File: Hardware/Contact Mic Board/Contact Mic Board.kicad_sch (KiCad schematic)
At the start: 29 parts, among them U1 ES8388, U2 MCP6002-xMC, U3 MCP6002-xMC

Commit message: revised contact mic board
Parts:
- removed C2, C4, C8: 0.1uF, symbol Device:C_Small
- removed C6: 10uF, symbol Device:C_Small
- removed R6: 100k, symbol Device:R
- added C15, C17, C2, C4, C6, C8: 10uF, symbol Device:C_Polarized_Small_US
- added C16, C18: 0.1uF, symbol Device:C_Small
- added FB1: FerriteBead_Small, symbol Device:FerriteBead_Small
- added J1: Conn_01x08_Pin, symbol Connector:Conn_01x08_Pin
- added R11, R12, R13, R14: 33, symbol Device:R_Small_US
- added R6: 100k, symbol Device:R_Small_US
- C5: value 4.7uF -> 0.1uF
- R1, R10, R2, R3, R4, R5, R7, R8, R9: symbol Device:R -> Device:R_Small_US
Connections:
- net GND: now also C1.1, C3.1, C5.1, C15.2, C16.2, C17.2, C18.2, C2.2, C4.2, C6.2, C8.2, J1.8 (Pin_8); no longer C1.2, C3.2, C5.2
- net at C11.2, C12.2, R3.2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: now also C17.1, C18.1
- net at U1.1 (MCLK): now also R11.2
- net at U1.27 (CDATA): now also J1.6 (Pin_6)
- net at U1.28 (CCLK): now also J1.7 (Pin_7)
- net at U1.5 (SCLK): now also R12.2
- net at U1.7 (LRCK): now also R13.2
- net at U1.8 (ASDOUT): now also R14.2
- net at C10.2, U2.1: now also R6.1
- net at R7.1, U2.2 (-): now also R6.2
- removed net +3.3V: C1.1, C3.1, C5.1, C7.2, U1.10 (VREF), U1.16 (HPVDD), U1.17 (AVDD), U1.19 (ADCVREF), U1.2 (DVDD), U1.3 (PVDD)
- new net: C8.1, U1.10 (VREF)
- new net: C1.2, C2.1, C3.2, C6.1, C7.2, FB1.2, J1.1 (Pin_1), U1.16 (HPVDD), U1.2 (DVDD), U1.3 (PVDD)
- new net: C4.1, C5.2, FB1.1, U1.17 (AVDD)
- new net: C15.1, C16.1, U1.19 (ADCVREF)
- new net: J1.2 (Pin_2), R11.1
- new net: J1.4 (Pin_4), R13.1
- new net: J1.3 (Pin_3), R12.1
- new net: J1.5 (Pin_5), R14.1
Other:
- moved on the sheet: C10, C9

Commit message: drafted contact mic pcb layout
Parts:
- removed U3: MCP6002-xMC, Package_DFN_QFN:DFN-8-1EP_3x2mm_P0.5mm_EP1.75x1.45mm, symbol Amplifier_Operational:MCP6002-xMC
- added unit 3 of U2
- added unit 2 of U2
- C1, C10, C11, C12, C13, C16, C18, C3, C9, R1, R10, R11, R12, R13, R14, R2, R3, R4, R7, R8, R9: footprint (none) -> Capacitor_SMD:C_0402_1005Metric
- C14: renamed from C8; footprint (none) -> Capacitor_SMD:C_0603_1608Metric
- C15, C17, C2, FB1: footprint (none) -> Capacitor_SMD:C_0603_1608Metric
- C4: renamed from C6; footprint (none) -> Capacitor_SMD:C_0603_1608Metric
- C5: renamed from C7; footprint (none) -> Capacitor_SMD:C_0402_1005Metric
- C6: renamed from C5; footprint (none) -> Capacitor_SMD:C_0402_1005Metric
- C7: renamed from C4; footprint (none) -> Capacitor_SMD:C_0603_1608Metric
- C8: renamed from C14; footprint (none) -> Capacitor_SMD:C_0402_1005Metric
- J1: value Conn_01x08_Pin -> Conn_01x09_Pin; footprint (none) -> Connector_JST:JST_GH_SM09B-GHS-TB_1x09-1MP_P1.25mm_Horizontal; symbol Connector:Conn_01x08_Pin -> Connector:Conn_01x09_Pin
- MIC1, MIC2: footprint (none) -> Connector_PinHeader_2.54mm:PinHeader_1x02_P2.54mm_Vertical
- R5, R6: footprint (none) -> Resistor_THT:R_Axial_DIN0207_L6.3mm_D2.5mm_P7.62mm_Horizontal
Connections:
- net GND: now also J1.1 (Pin_1), J1.3 (Pin_3), U2.4 (V-), U2.9 (V-); no longer J1.8 (Pin_8)
- net at C9.2, R5.2: now also U2.7
- net at R5.1, R8.1: now also U2.6 (-)
- net at C1.2, C2.1, C3.2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: now also J1.9 (Pin_9); no longer C4.1, C5.2, J1.1 (Pin_1), U1.16 (HPVDD)
- net at C6.2, C7.1, FB1.1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: now also C4.1, C5.2, U1.16 (HPVDD), U2.8 (V+)
- net at U1.27 (CDATA): now also J1.7 (Pin_7); no longer J1.6 (Pin_6)
- net at U1.28 (CCLK): now also J1.8 (Pin_8); no longer J1.7 (Pin_7)
- net at R2.1, R4.1: now also U2.5 (+)
- net at R11.1: now also J1.6 (Pin_6); no longer J1.2 (Pin_2)
- net at R12.1: now also J1.2 (Pin_2); no longer J1.3 (Pin_3)
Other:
- moved on the sheet: C12, R6, R7

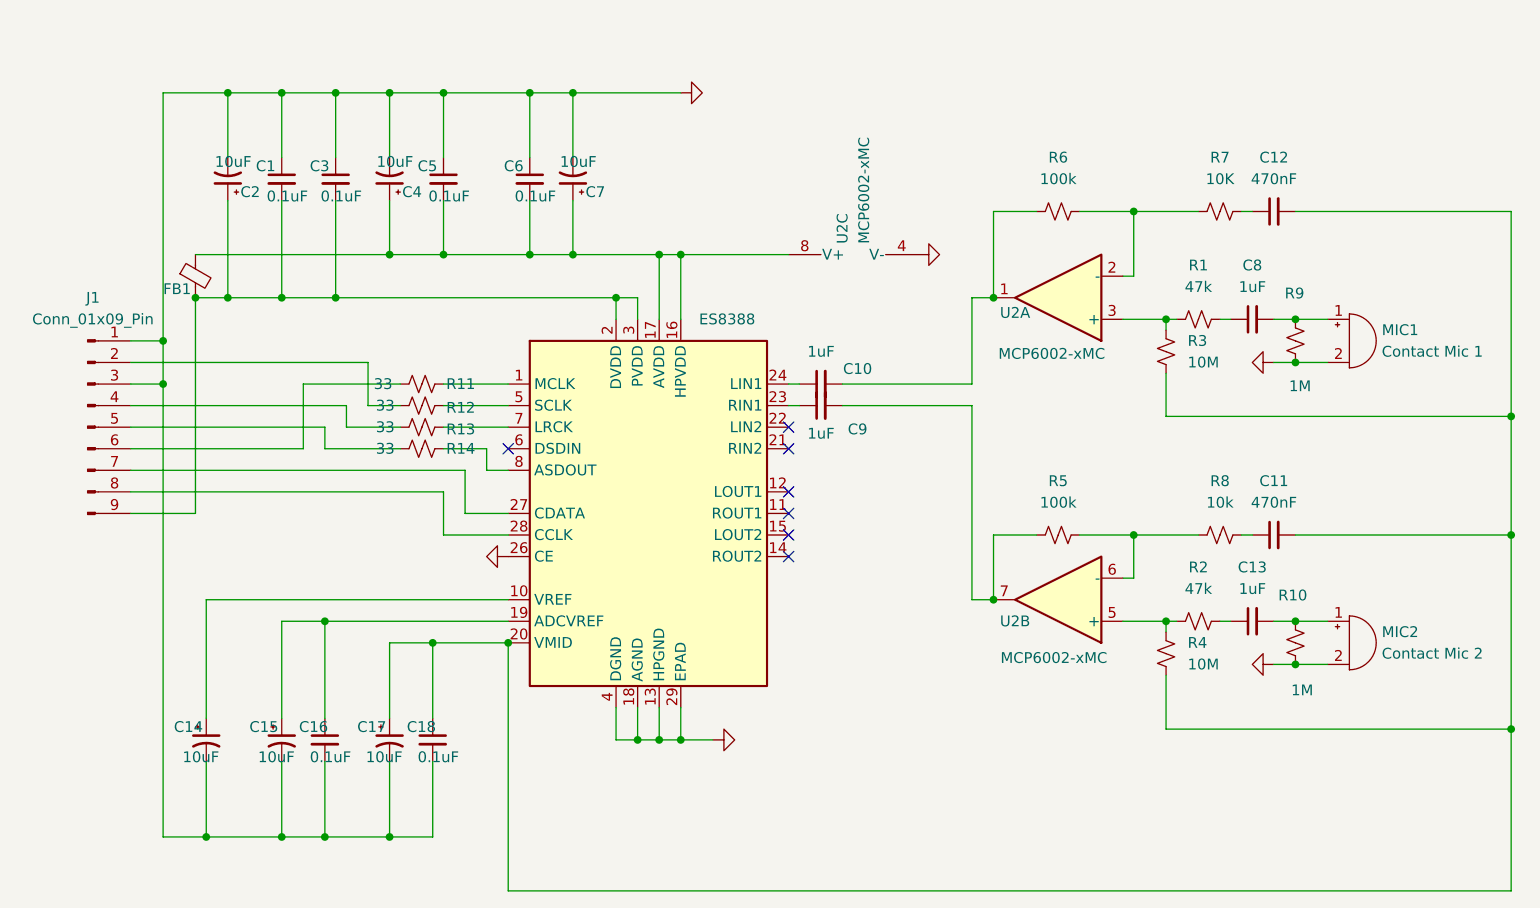
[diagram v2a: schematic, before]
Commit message: Finalized layout for contact mic board
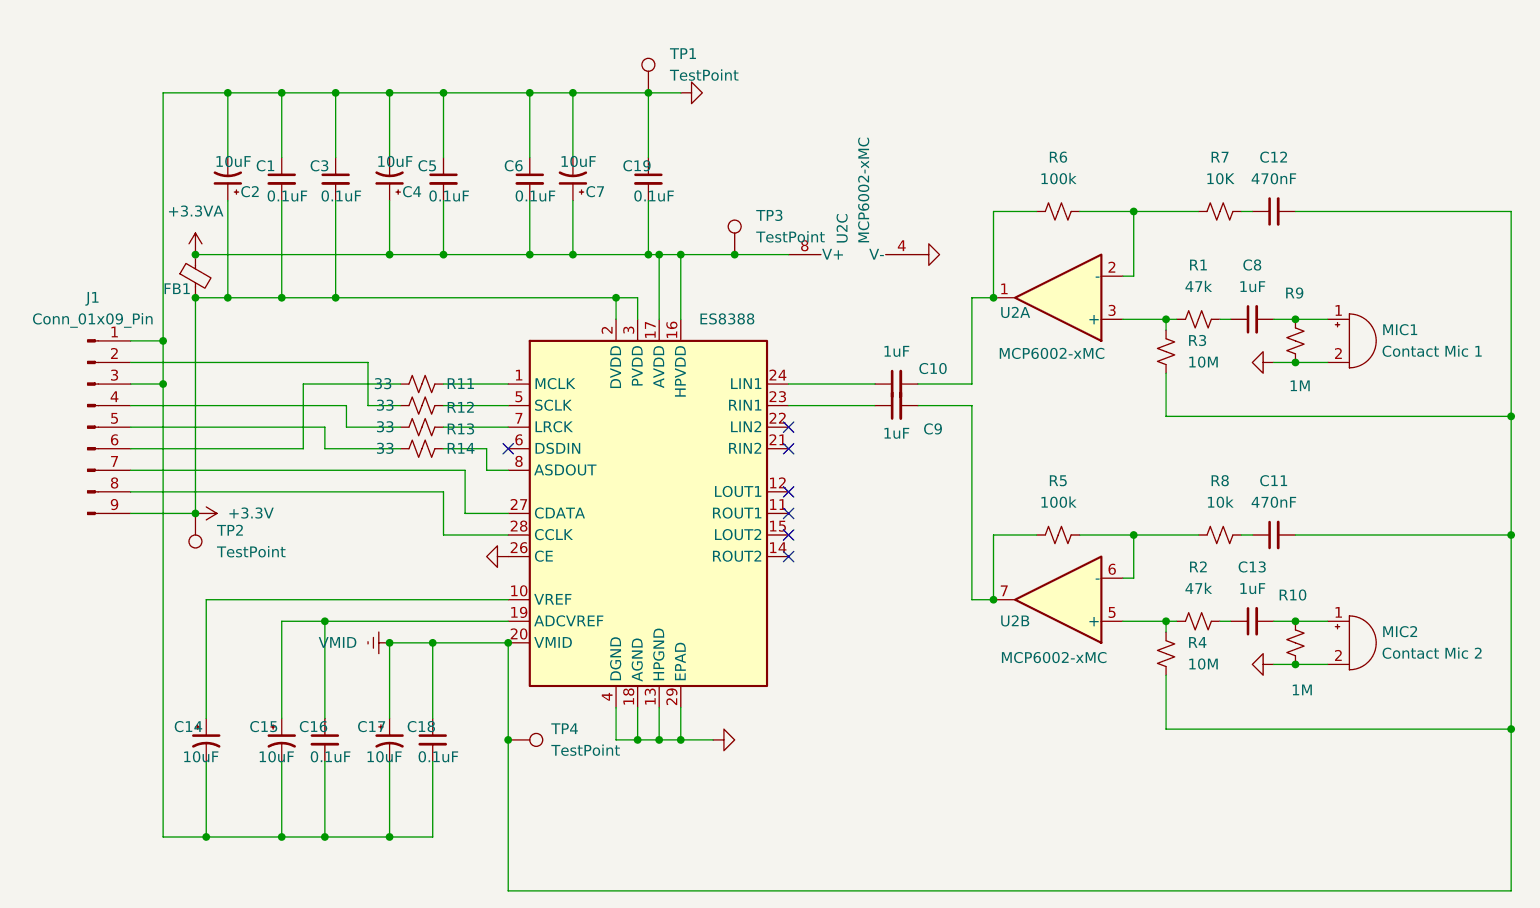
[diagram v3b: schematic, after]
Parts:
- added C19: 0.1uF, Capacitor_SMD:C_0402_1005Metric, symbol Device:C_Small
- added TP1, TP2, TP3, TP4: TestPoint, TestPoint:TestPoint_Pad_1.0x1.0mm, symbol Connector:TestPoint
- C14, C15, C17, C2, C4, C7: footprint Capacitor_SMD:C_0603_1608Metric -> Capacitor_SMD:C_0402_1005Metric
- R5, R6: footprint Resistor_THT:R_Axial_DIN0207_L6.3mm_D2.5mm_P7.62mm_Horizontal -> Diode_SMD:D_0805_2012Metric_Pad1.15x1.40mm_HandSolder
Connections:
- net GND: now also C19.1, TP1.1
- net VMID: now reaches C11.2, C12.2, C17.1, C18.1, R3.2, R4.2, U1.20 (VMID)
- net VMID: now also TP4.1
- net +3.3VA: now reaches C4.1, C5.2, C6.2, C7.1, FB1.1, U1.16 (HPVDD), U1.17 (AVDD), U2.8 (V+)
- net +3.3VA: now also C19.2, TP3.1
- net +3.3V: now reaches C1.2, C2.1, C3.2, FB1.2, J1.9 (Pin_9), U1.2 (DVDD), U1.3 (PVDD)
- net +3.3V: now also TP2.1
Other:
- moved on the sheet: C10, C9

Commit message: separated the microphone onto its own schematic as we won't be designing it. Updated the contact mic board
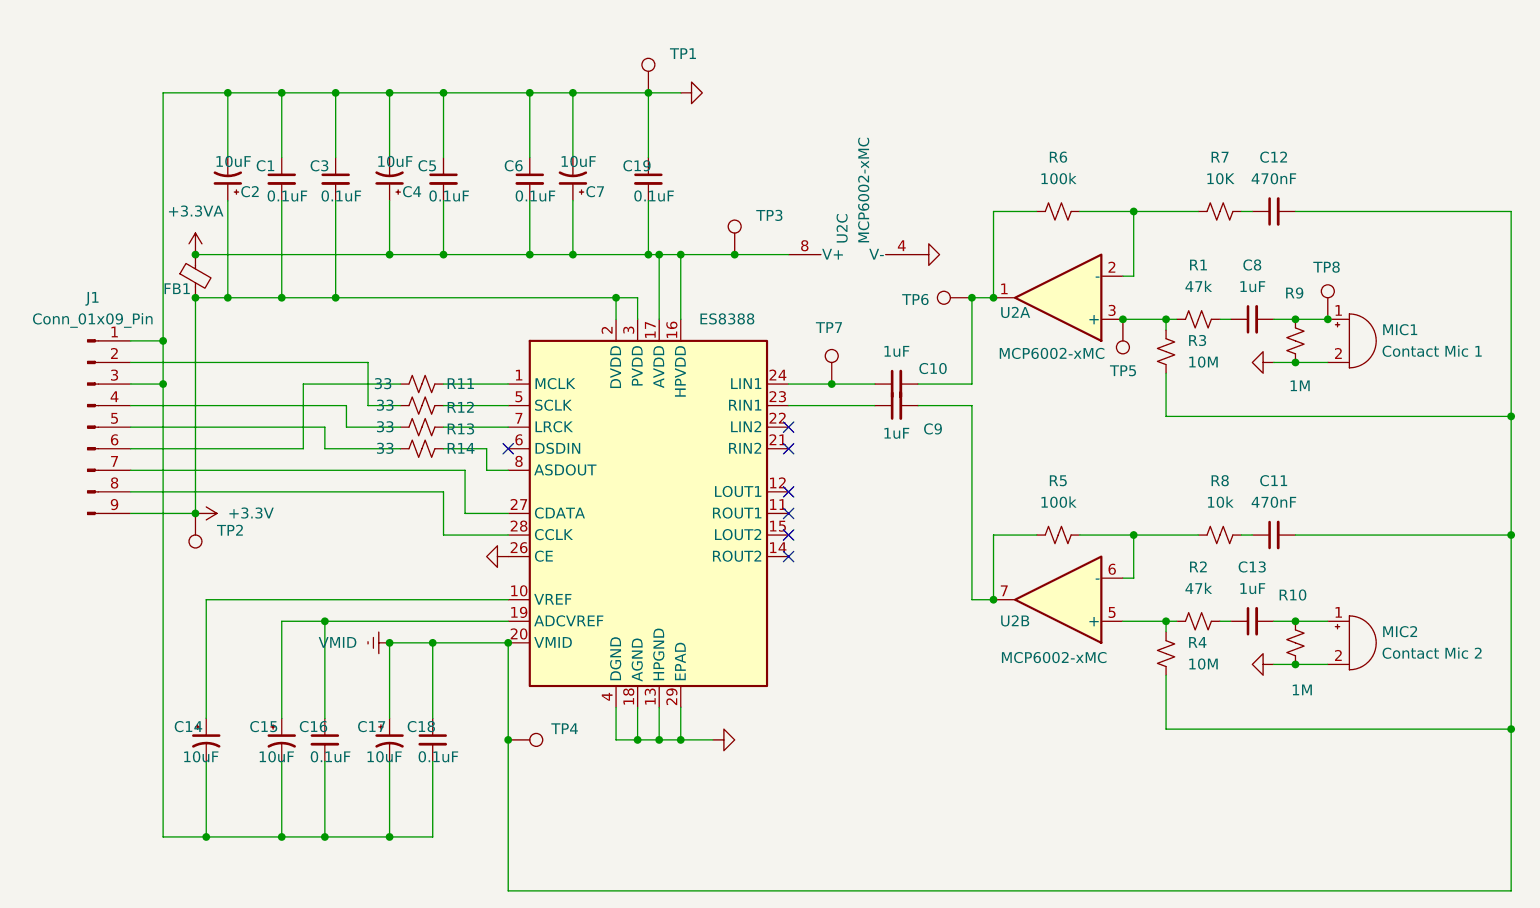
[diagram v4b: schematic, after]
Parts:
- added TP5, TP6, TP7, TP8: TestPoint, TestPoint:TestPoint_Pad_1.0x1.0mm, symbol Connector:TestPoint
- MIC1, MIC2, TP1, TP2, TP3, TP4: now left out of the parts list
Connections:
- net at C8.2, MIC1.1 (+), R9.1: now also TP8.1
- net at C10.1, U1.24 (LIN1): now also TP7.1
- net at C10.2, R6.1, U2.1: now also TP6.1
- net at R1.1, R3.1, U2.3 (+): now also TP5.1
